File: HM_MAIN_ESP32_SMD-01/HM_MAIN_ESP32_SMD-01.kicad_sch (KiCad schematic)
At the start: 7 parts, among them J1 Conn_01x04_Pin, J2 Conn_02x19_Odd_Even, M2 ESP32-WROOM, SW1 SW_Push, SW2 SW_Push

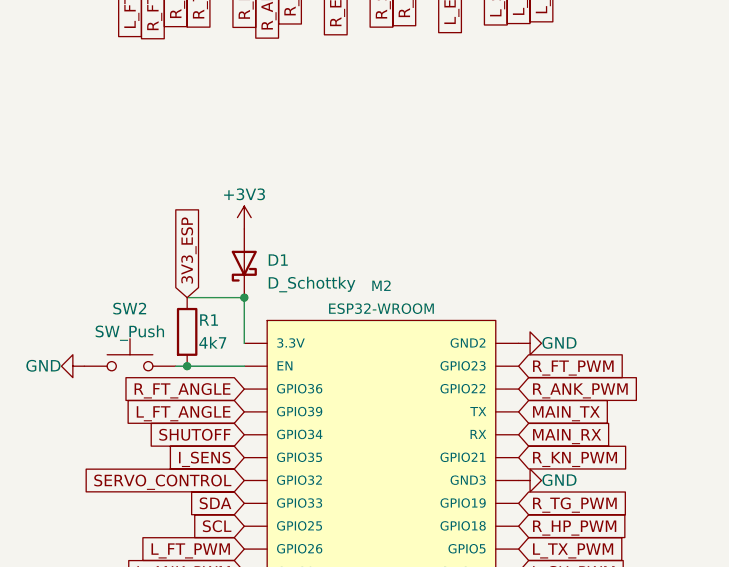
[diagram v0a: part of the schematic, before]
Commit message: arrumado código de teste do MPU e modelo dos diodos adicionado
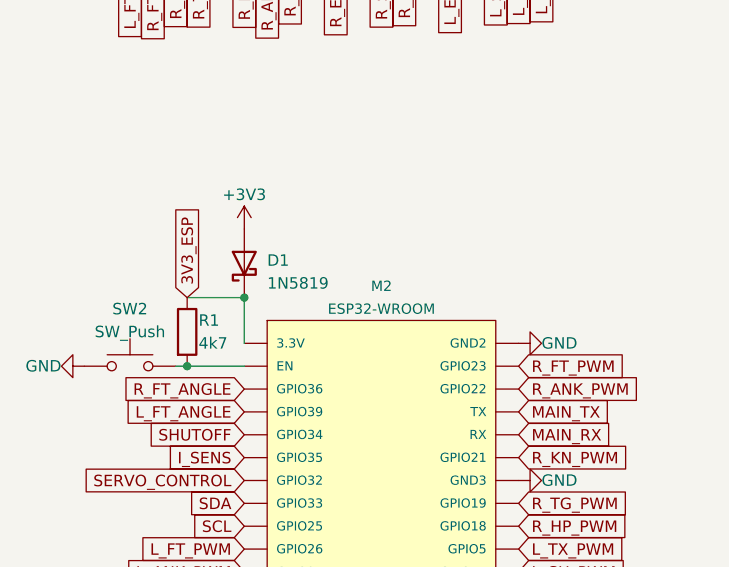
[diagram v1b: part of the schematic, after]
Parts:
- D1: value D_Schottky -> 1N5819
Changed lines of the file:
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@@
       (effects (font (size 1.27 1.27)) (justify right))
     )
-    (property "Value" "D_Schottky" (at 50.8 91.1225 90)
+    (property "Value" "1N5819" (at 50.8 91.1225 90)
       (effects (font (size 1.27 1.27)) (justify right))
     )
